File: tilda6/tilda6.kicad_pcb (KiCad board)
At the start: 2 copper layers, 60 x 23.5 mm, 44 parts, among them J1 Conn_02x14_Odd_Even, J2 Conn_02x02_Odd_Even, J3 Conn_02x02_Odd_Even, P1 USB_C_Plug, Q1 LP0404N3T5G, Q2 2SK3019, Q3 LP0404N3T5G, SW1 SW_SPDT, SW2 SW_SPST, SW3 SW_SPST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

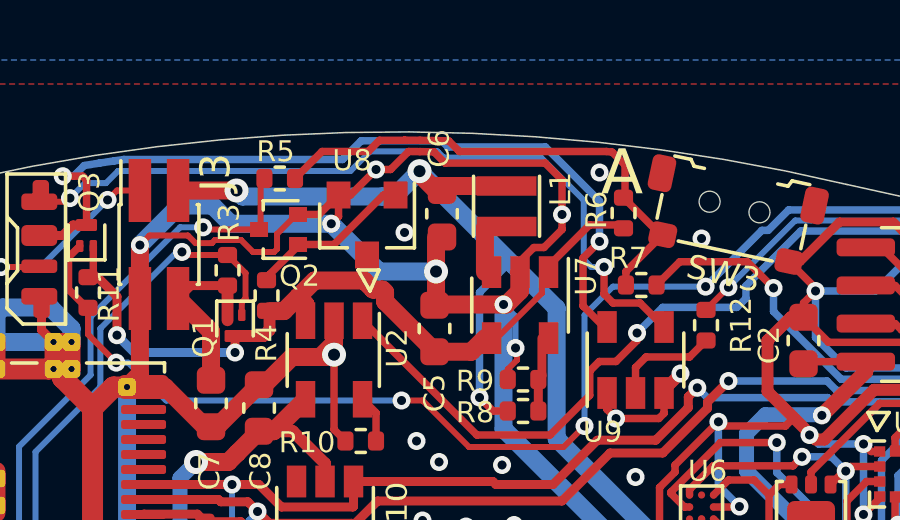
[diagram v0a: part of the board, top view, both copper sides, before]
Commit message: Add remaining 3d models, fix L1 fp
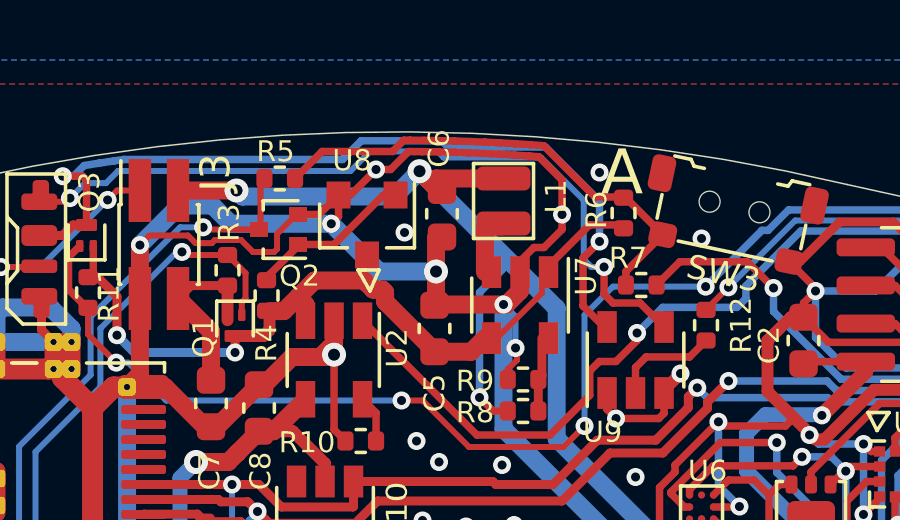
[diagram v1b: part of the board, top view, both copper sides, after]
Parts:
- L1: footprint Inductor_SMD:L_Taiyo-Yuden_MD-2020 -> tilda6:MHCHL201610A-2R2M-Q8A
- moved L1 0.20 mm to (118.5, 100.5)
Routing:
- net Net-(R5-Pad2): track 16.9 -> 16.2 mm

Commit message: Change DC/DC to M3406-ADJ for lower quiescent current at low load
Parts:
- U7: value MT3520B -> M3406-ADJ

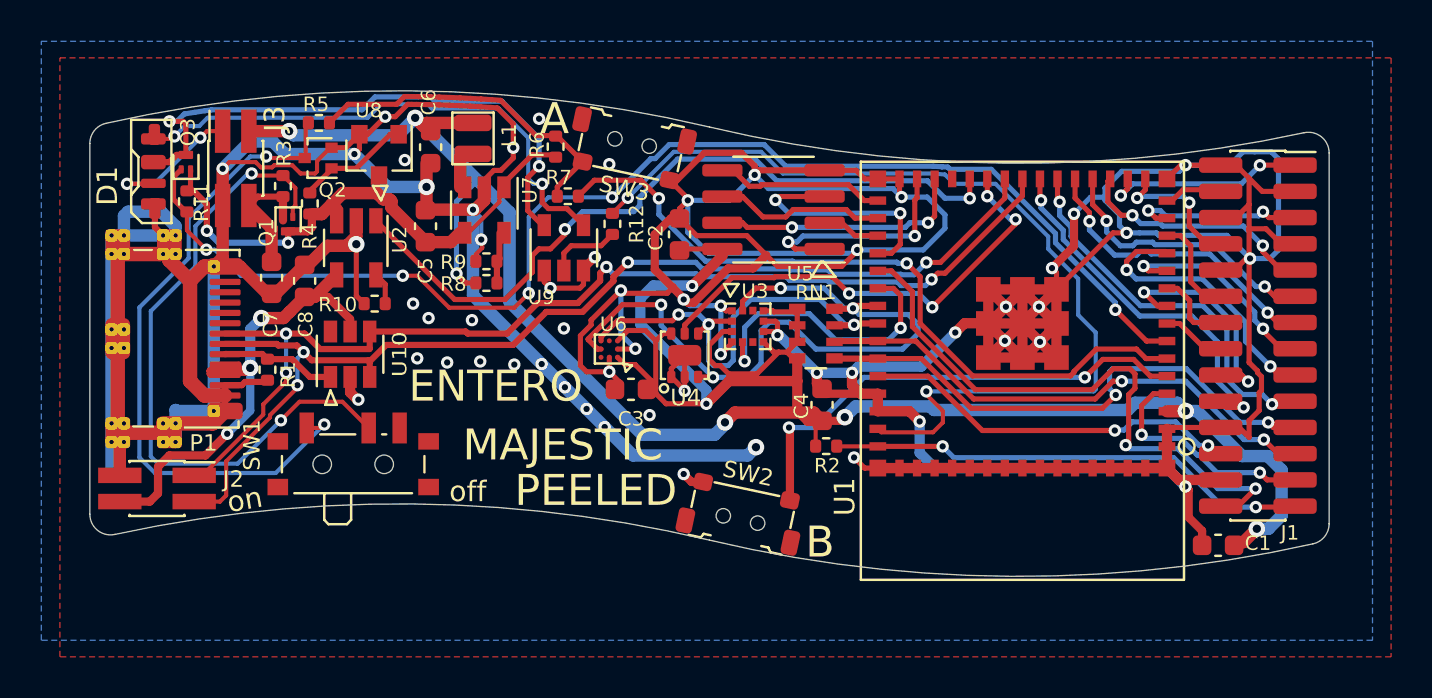
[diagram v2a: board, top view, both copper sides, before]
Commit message: Implement most of martling's recommendations: - power switch now controls DC/DC enable - top board caps changed from 1x4.7u to 1x1u+1x10n - top board edge via stitching - bottom board ground all around edge where possible - changed UVLO monitor threshold to 3.3V - all outermost traces very close to edge are now gnd not implemented: VBUS ferrite
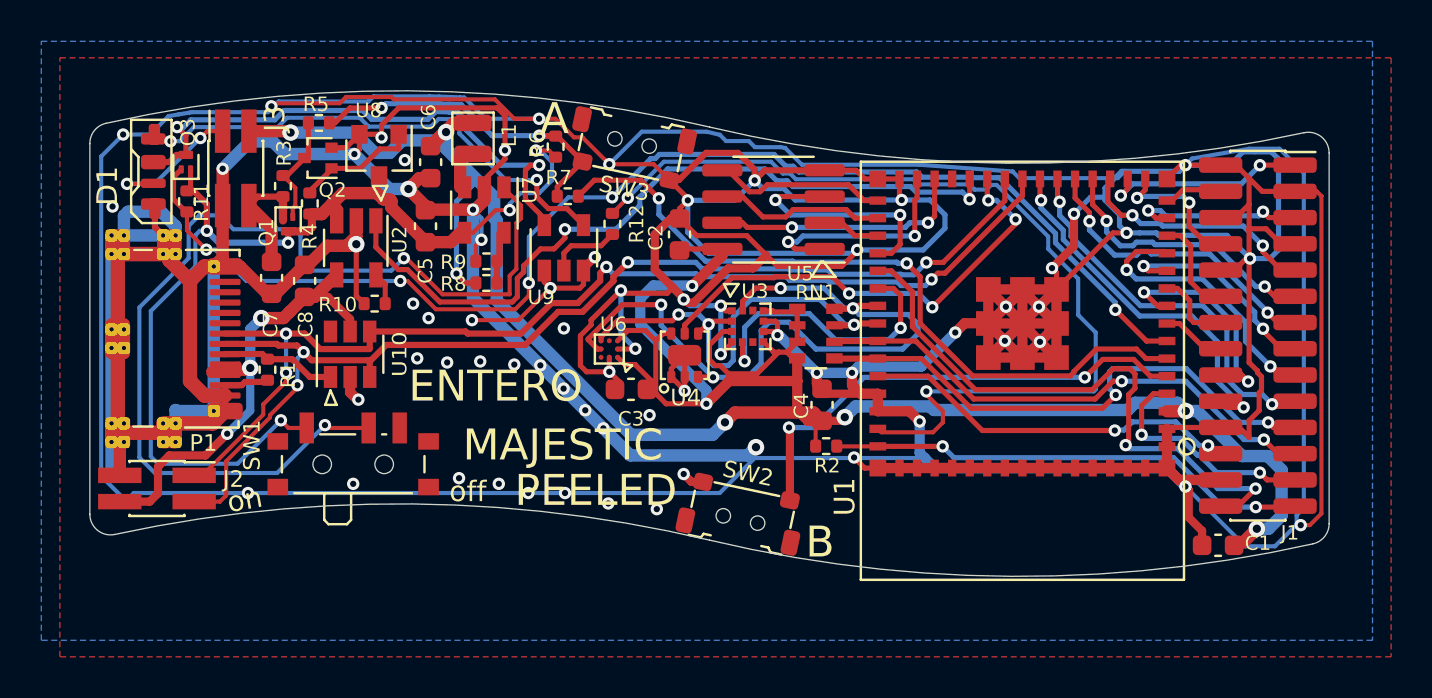
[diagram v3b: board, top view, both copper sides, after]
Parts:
- C1, C2, C3, C4, C5, C6, C7, C8: value C -> 4.7u
- U8: value SSP61CC3002MR -> ME2807A33M3G
- moved C6 0.73 mm to (116.5, 101.7)
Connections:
- Q2 pad 3: Net-(Q2-Pad3) -> Net-(Q1-Pad1)
- R5 pad 1: Net-(Q2-Pad3) -> Net-(Q1-Pad1)
- SW1 pad 1: Net-(Q2-Pad3) -> /VBAT_SW
- SW1 pad 2: Net-(Q1-Pad1) -> Net-(SW1-Pad2)
- SW1 pad 3: Net-(SW1-Pad3) -> GND
- U7 pad 1: /VBAT_SW -> Net-(SW1-Pad2)
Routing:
- net GND: track 405.7 -> 578.9 mm, vias 55 -> 67
- net Net-(SW1-Pad2): track 0.00 -> 49.0 mm, vias 0 -> 2
- net Net-(Q2-Pad3): track 32.4 -> 0.00 mm, vias 2 -> 0
- net Net-(Q1-Pad1): track 32.1 -> 5.48 mm, vias 2 -> 0
- net /VBAT_SW: track 27.4 -> 50.7 mm, vias 2 -> 5
- net /VLED: track 28.0 -> 26.6 mm
- net /3V3: track 125.8 -> 127.2 mm
- net Net-(D1-Pad4): track 25.6 -> 24.5 mm
- net /CHARGE_DET: track 35.7 -> 36.6 mm
- net /LED_PWR: track 62.2 -> 61.4 mm
- net Net-(R5-Pad2): track 16.2 -> 16.8 mm, vias 0 -> 2
